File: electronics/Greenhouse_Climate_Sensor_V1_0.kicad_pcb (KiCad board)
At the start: 2 copper layers, 9 parts, among them U1 NodeMCU_1.0_(ESP-12E), U2 DHT22, U3 AMS1117-3.3

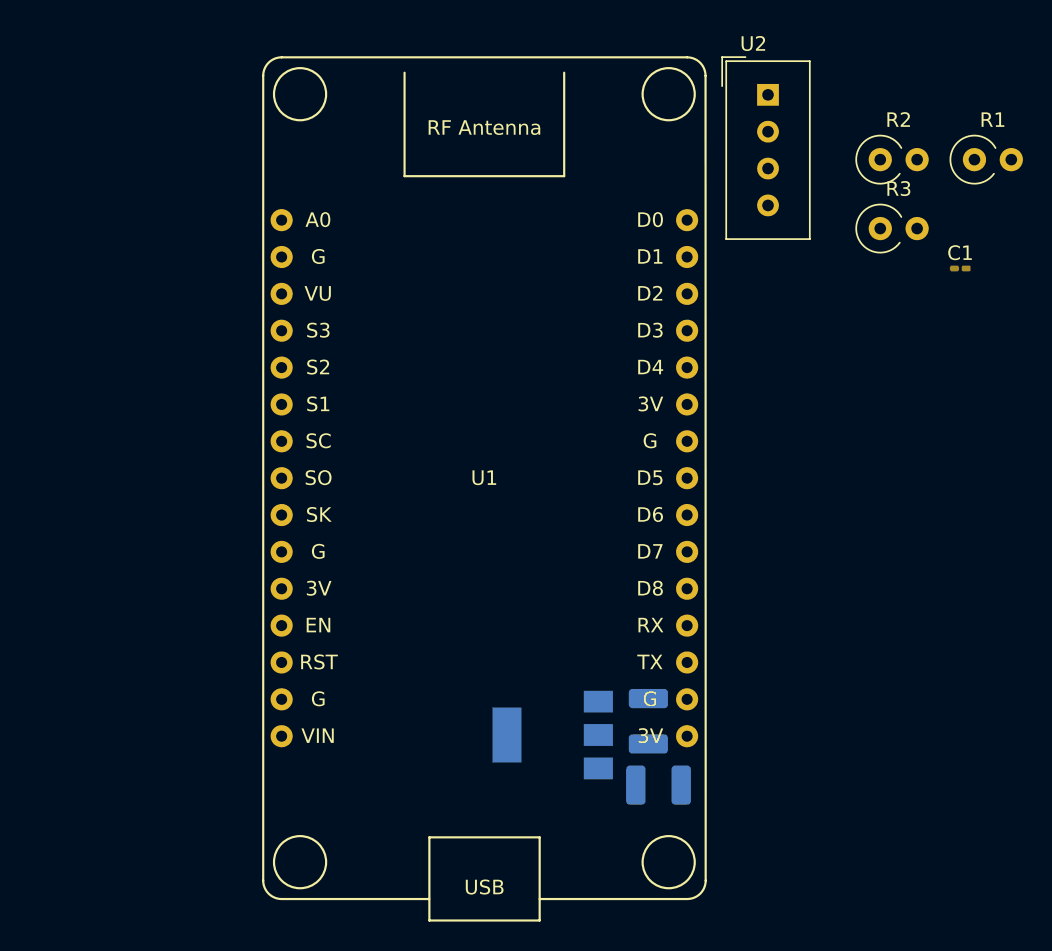
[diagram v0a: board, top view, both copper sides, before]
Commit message: add minimally functional firmware. Probably final changes to hardware
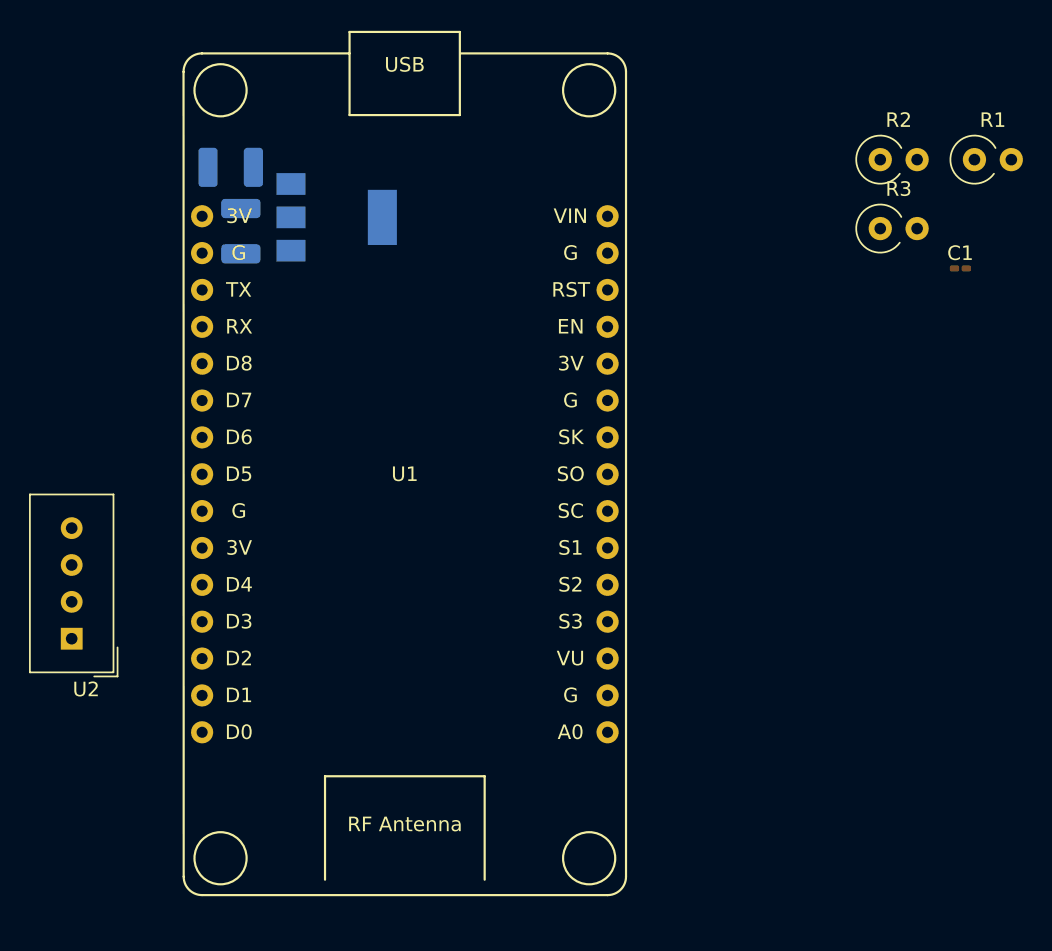
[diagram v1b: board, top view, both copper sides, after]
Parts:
- moved U2 60.9 mm to (73.6, 79.9), turned to 180 degrees
- moved C2 51.8 mm to (84.5, 47.4), turned to 180 degrees
- moved C3 43.9 mm to (85.2, 51.8), turned to -90 degrees
- moved U3 38.6 mm to (91.8, 50.9), turned to 0 degrees
- moved U1 5.49 mm to (96.5, 68.6), turned to 180 degrees
